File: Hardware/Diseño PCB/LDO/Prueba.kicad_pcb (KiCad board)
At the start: 2 copper layers, 100 x 100 mm, 55 parts, among them Q1 2N3904, Q10 BC557, Q11 BC547, Q12 BC557, Q13 2N3906, Q14 2N3904, Q15 2N3906, Q16 2N3904, Q17 2N3906, Q18 2N3904, Q19 2N3904, Q2 2N3904, Q3 2N3904, Q4 2N3906, Q5 2N3906, Q6 2N3904, Q7 2N3904, Q8 IRF4905, Q9 BC547, U1 TL431LP, U4 LM324

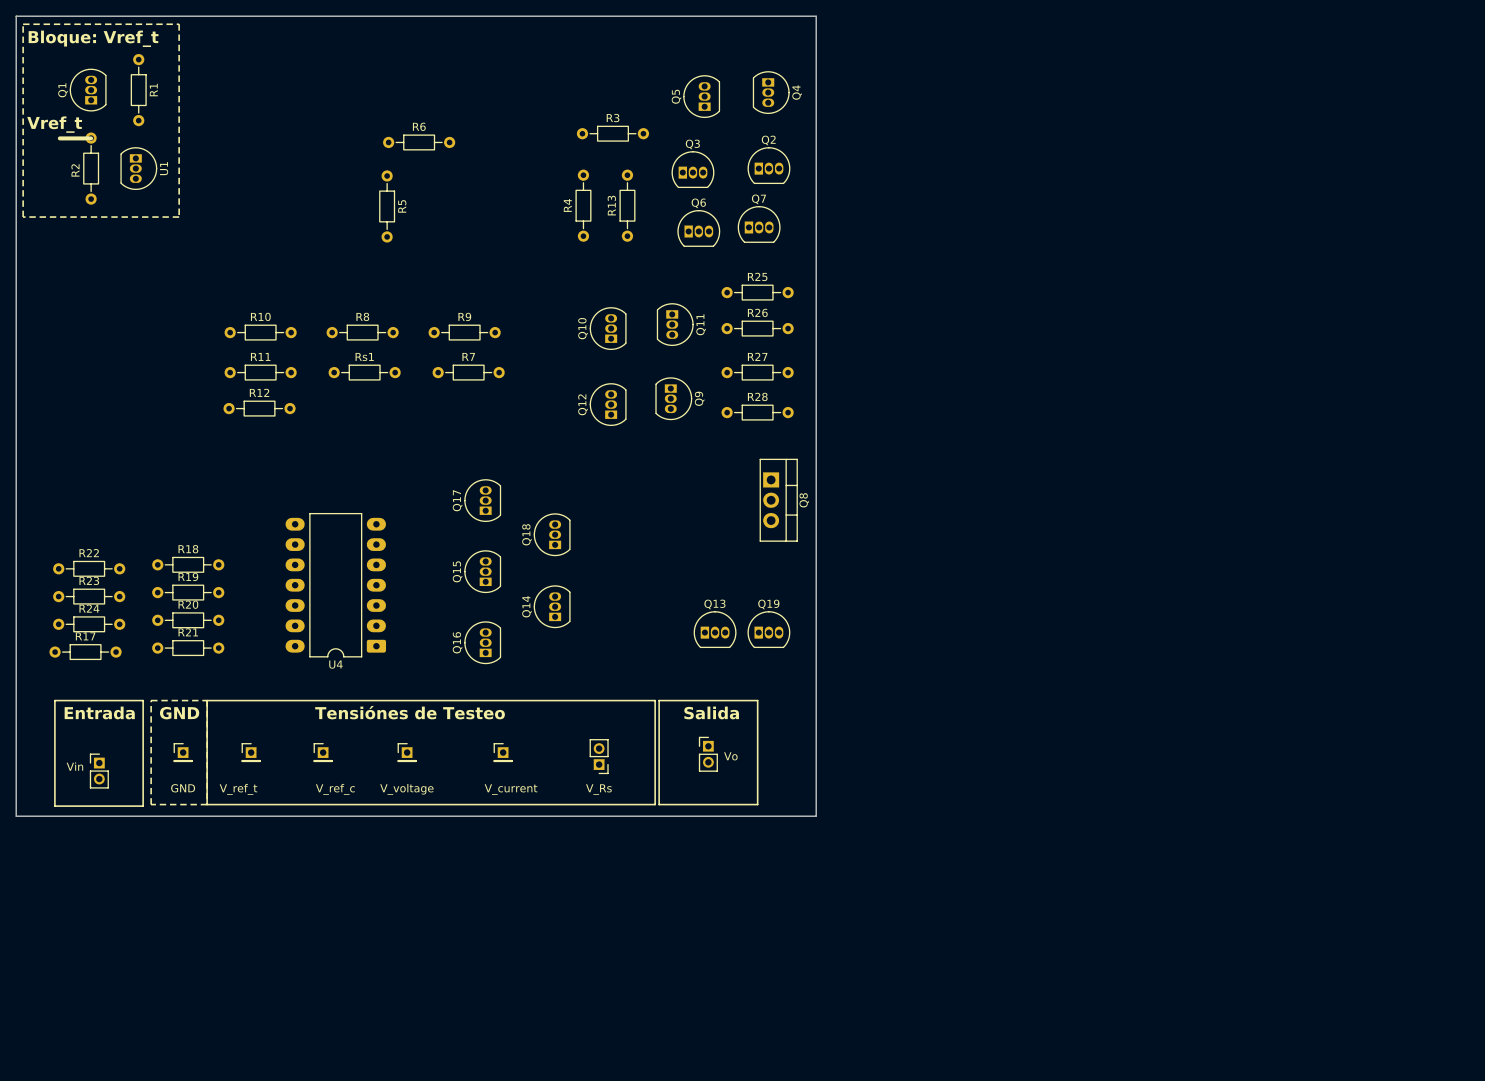
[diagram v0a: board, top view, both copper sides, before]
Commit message: Diseño PCB : Bloque testeos y Vref_t
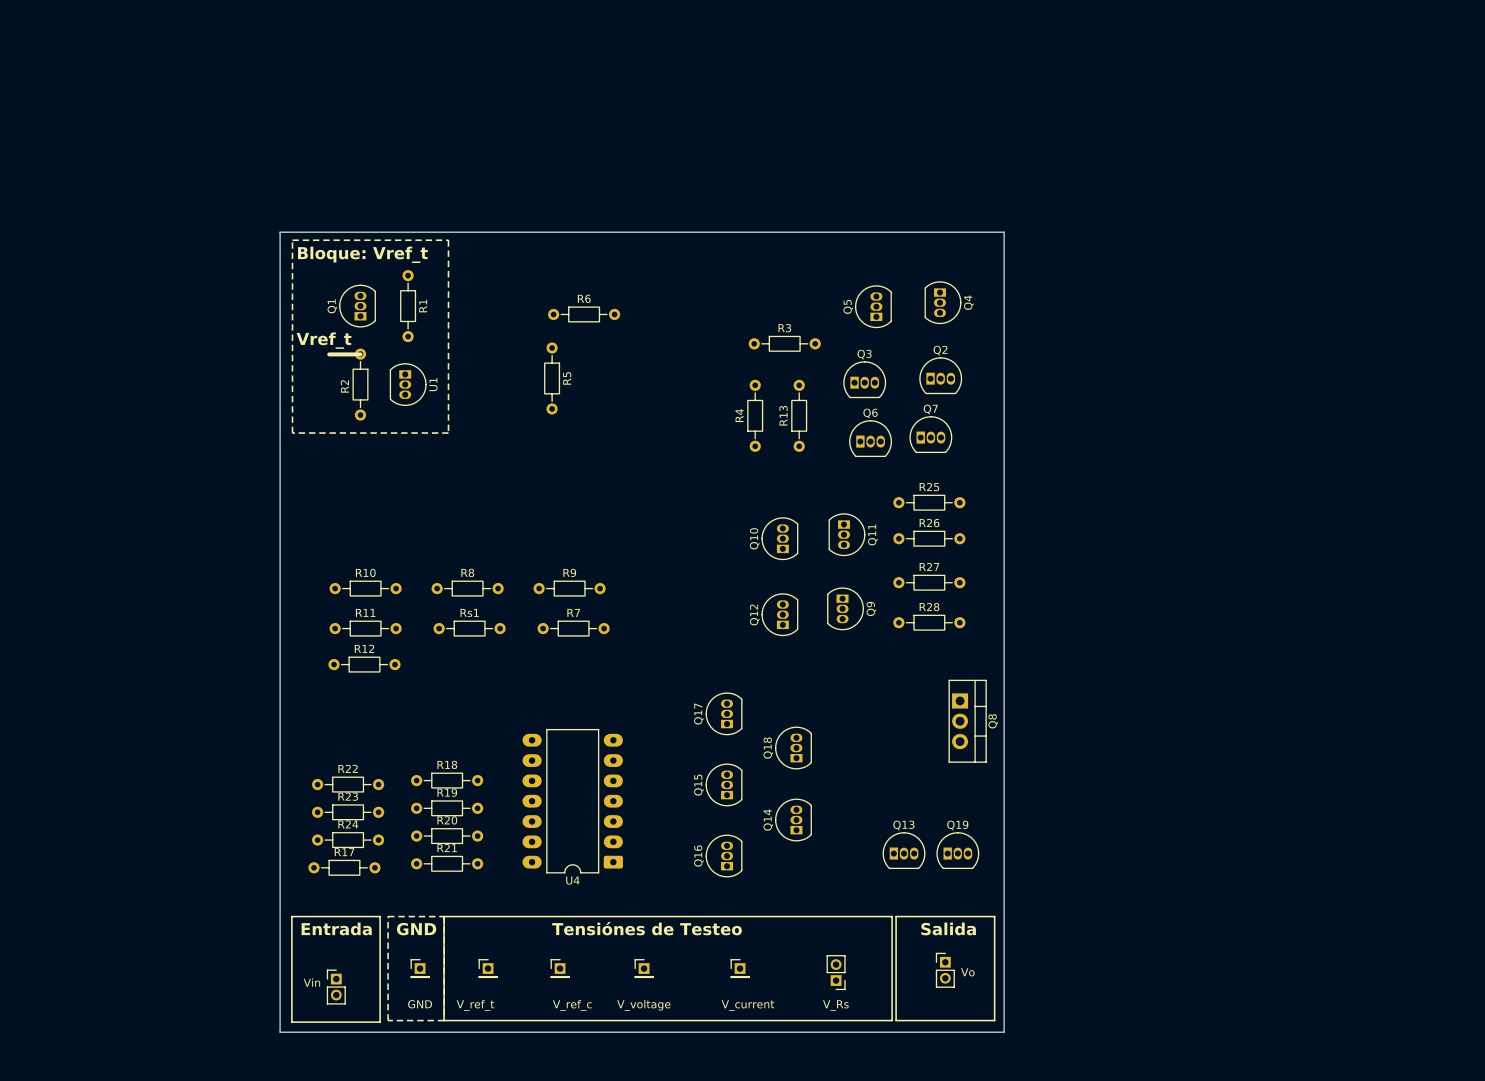
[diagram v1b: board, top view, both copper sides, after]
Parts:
- moved R1 43.2 mm to (118.6, 47.9)
- moved U1 43.2 mm to (118.3, 60.2)
- moved Q1 43.2 mm to (112.7, 53.0)
- moved R2 43.2 mm to (112.7, 57.7)
- moved R24 42.1 mm to (107.3, 118.4)
- moved R17 42.1 mm to (106.9, 121.9)
- moved R22 42.1 mm to (107.3, 111.5)
- moved R23 42.1 mm to (107.3, 115.0)
- moved R20 42.1 mm to (119.7, 117.9)
- moved R18 42.1 mm to (119.7, 111.0)
- moved R19 42.1 mm to (119.7, 114.5)
- moved R21 42.1 mm to (119.7, 121.4)
- moved Q15 40.3 mm to (158.5, 112.8)
- moved Q17 40.3 mm to (158.5, 103.9)
- moved Q14 40.3 mm to (167.2, 117.2)
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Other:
- board size 100 x 100 mm -> 90.5 x 100 mm

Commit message: Diseño PCB
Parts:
- moved R28 35.3 mm to (187.5, 56.8), turned to 90 degrees
- moved Q12 34.1 mm to (186.8, 65.0)
- moved R27 29.6 mm to (182.5, 56.8), turned to 90 degrees
- moved Q4 26.5 mm to (159.0, 45.5)
- moved R26 24.1 mm to (177.0, 56.8), turned to 90 degrees
- moved Q10 22.7 mm to (177.4, 62.7), turned to -90 degrees
- moved Q9 19.9 mm to (177.6, 69.0)
- moved Q6 18.3 mm to (158.8, 60.5)
- moved Q3 18.1 mm to (159.1, 51.6), turned to -90 degrees
- moved Q7 18.1 mm to (166.4, 60.5)
- moved R4 17.8 mm to (145.4, 62.9)
- moved R3 17.8 mm to (145.3, 50.1)
- moved Q2 17.1 mm to (168.1, 54.1), turned to 90 degrees
- moved R13 16.2 mm to (152.6, 62.9)
- moved Q11 15.6 mm to (186.8, 71.5), turned to 90 degrees
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
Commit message: Diseño PCB
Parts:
- moved R10 106.4 mm to (215.2, 75.0)
- moved R11 106.4 mm to (215.2, 80.0)
- moved R12 106.4 mm to (215.1, 84.5)
- moved R18 106.4 mm to (225.4, 99.0)
- moved R19 106.4 mm to (225.4, 102.5)
- moved R20 106.4 mm to (225.4, 105.9)
- moved R21 106.4 mm to (225.4, 109.4)
- moved R22 106.4 mm to (213.0, 99.5)
- moved R23 106.4 mm to (213.0, 103.0)
- moved R24 106.4 mm to (213.0, 106.4)
- moved R7 106.4 mm to (241.2, 80.0)
- moved R8 106.4 mm to (228.0, 75.0)
- moved R9 106.4 mm to (240.7, 75.0)
- moved Rs1 106.4 mm to (228.2, 80.0)
- moved U4 106.4 mm to (250.0, 109.2)
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
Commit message: Diseño PCB
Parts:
- moved R18 120.5 mm to (106.0, 115.0)
- moved LM324 119.4 mm to (130.6, 112.7)
- moved R12 115.0 mm to (106.0, 121.0)
- moved R9 113.6 mm to (136.8, 121.0)
- moved R7 107.4 mm to (140.0, 116.0)
- moved R23 107.3 mm to (106.0, 96.0)
- moved R11 107.2 mm to (116.2, 121.0)
- moved R24 107.1 mm to (106.0, 102.0)
- moved R17 106.6 mm to (106.0, 108.5)
- moved R20 104.8 mm to (121.8, 90.0)
- moved R10 100.2 mm to (126.2, 121.0)
- moved R8 94.2 mm to (140.0, 108.6)
- moved R19 85.9 mm to (140.4, 90.0), turned to 180 degrees
- moved R21 84.3 mm to (142.3, 95.0)
- moved Rs1 83.3 mm to (150.0, 108.5), turned to -90 degrees
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- renumbered U4 to LM324
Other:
- board size 90.5 x 100 mm -> 90.5 x 92.5 mm
- board text added: "Grupo 7: Regulador de baja caída (LDO,Low Dropout Regulator)"

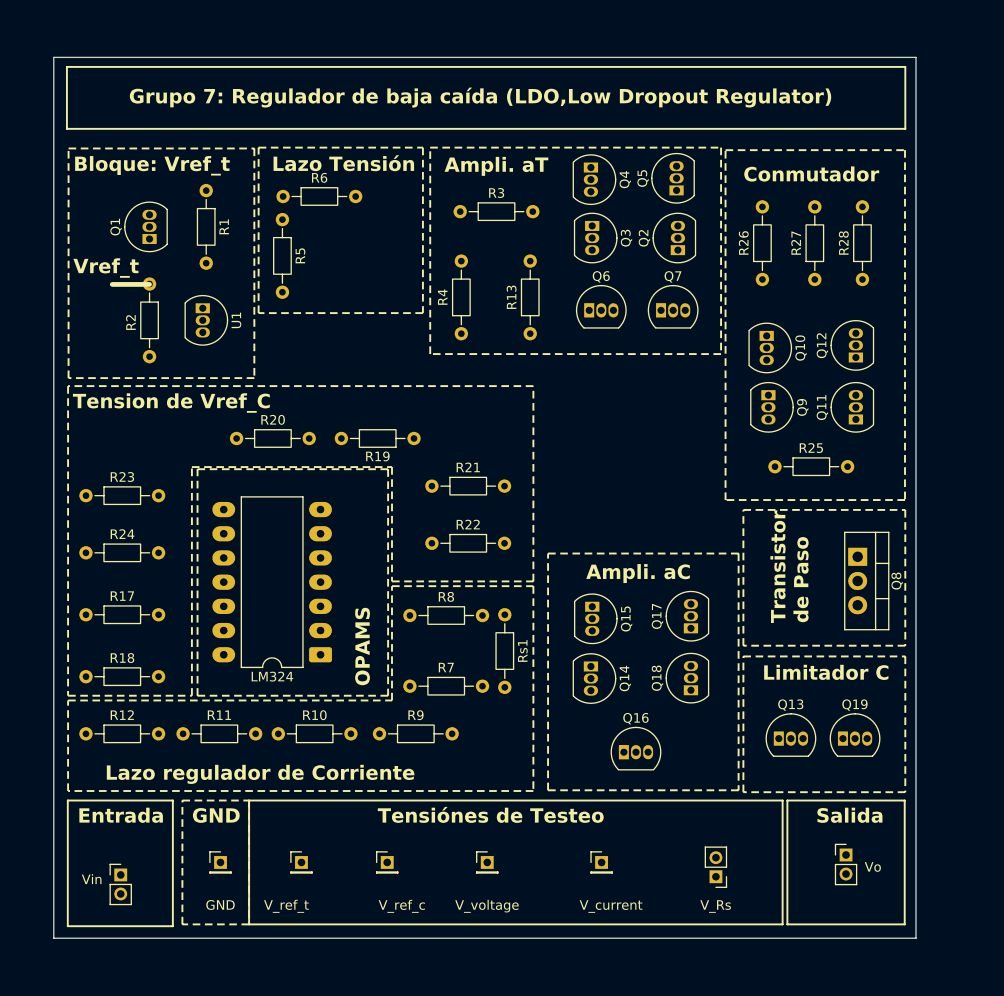
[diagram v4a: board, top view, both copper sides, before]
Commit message: Diseño PCB: Informe, orificos de sujeción
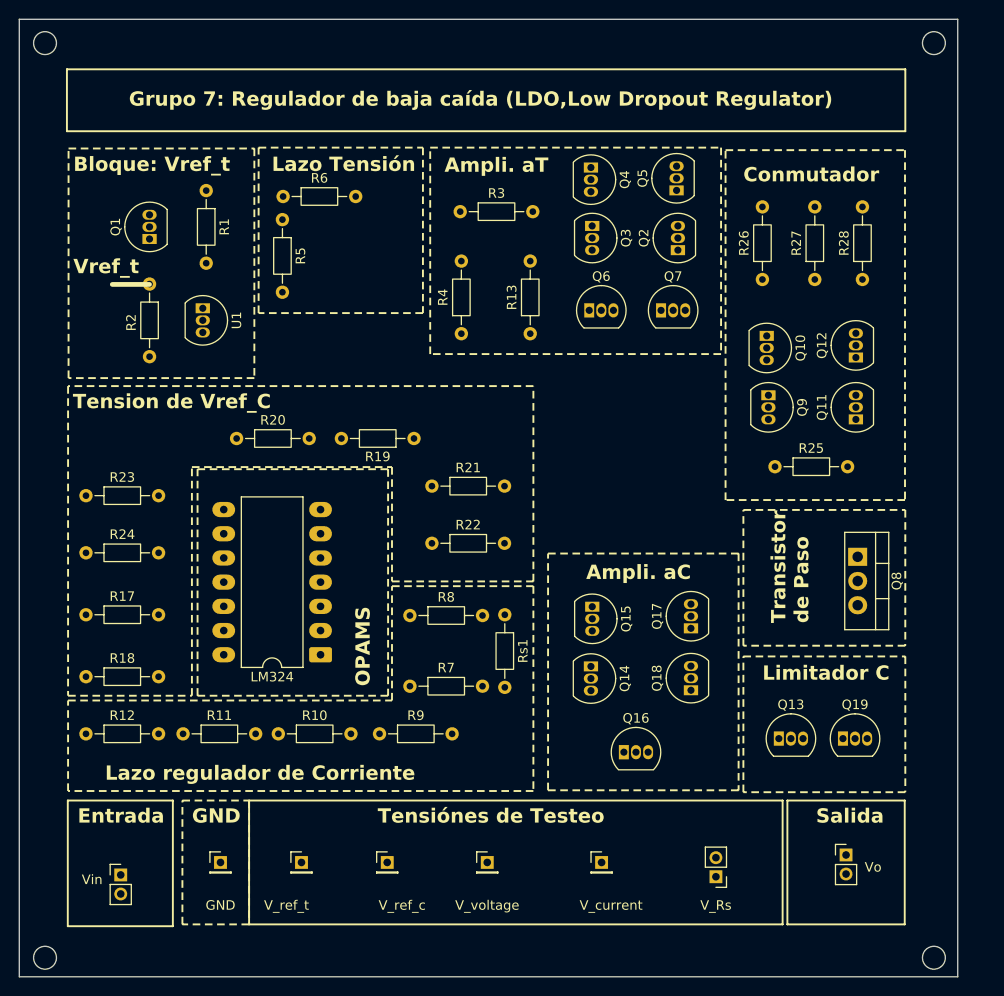
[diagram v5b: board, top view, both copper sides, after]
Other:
- board size 90.5 x 92.5 mm -> 98.5 x 100.5 mm
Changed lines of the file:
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@@
 	)
 	(gr_rect
-		(start 104 51)
-		(end 192 57.499999)
+		(start 104 51.25)
+		(end 192 57.749999)
 		(stroke
 			(width 0.2)
@@
 	)
 	(gr_rect
-		(start 102.619999 50)
-		(end 193.119999 142.45256)
+		(start 98.999999 46)
+		(end 197.499999 146.5)
 		(stroke
 			(width 0.05)
+			(type solid)
+		)
+		(fill no)
+		(layer "Edge.Cuts")
+	)
+	(gr_circle
+		(center 101.7 48.5)
+		(end 102.9 48.5)
+		(stroke
+			(width 0.1)
+			(type solid)
+		)
+		(fill no)
+		(layer "Edge.Cuts")
+	)
+	(gr_circle
+		(center 101.7 144.5)
+		(end 102.9 144.5)
+		(stroke
+			(width 0.1)
+			(type solid)
+		)
+		(fill no)
+		(layer "Edge.Cuts")
+	)
+	(gr_circle
+		(center 195 48.5)
+		(end 196.2 48.5)
+		(stroke
+			(width 0.1)
+			(type solid)
+		)
+		(fill no)
+		(layer "Edge.Cuts")
+	)
+	(gr_circle
+		(center 195 144.5)
+		(end 196.2 144.5)
+		(stroke
+			(width 0.1)
 			(type solid)
 		)
@@
 	)
 	(gr_text "Grupo 7: Regulador de baja caída (LDO,Low Dropout Regulator)"
-		(at 110.5 55 0)
-		(layer "F.SilkS")
-		(effects
+		(at 110.5 55.25 0)
+		(layer "F.SilkS")
+		(effects

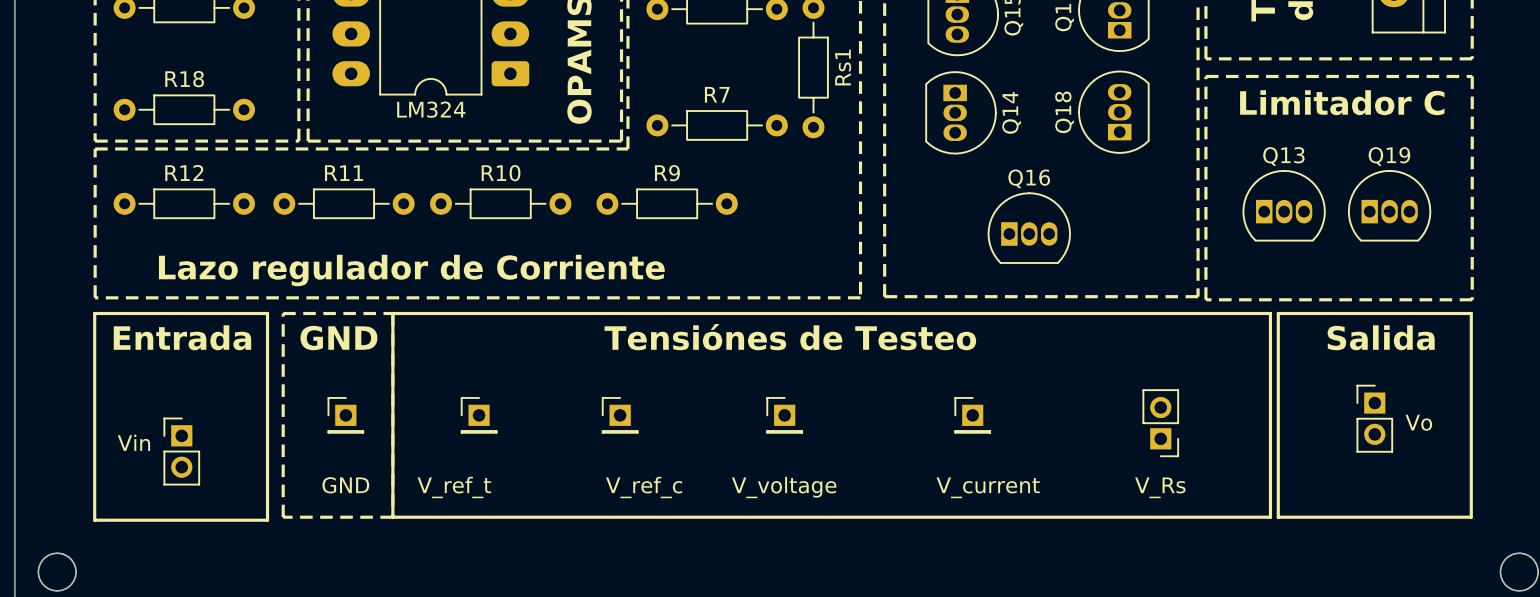
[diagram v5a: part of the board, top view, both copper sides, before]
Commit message: Diseño PCB: Transistores BC557/BC547 en esquematico y pcb
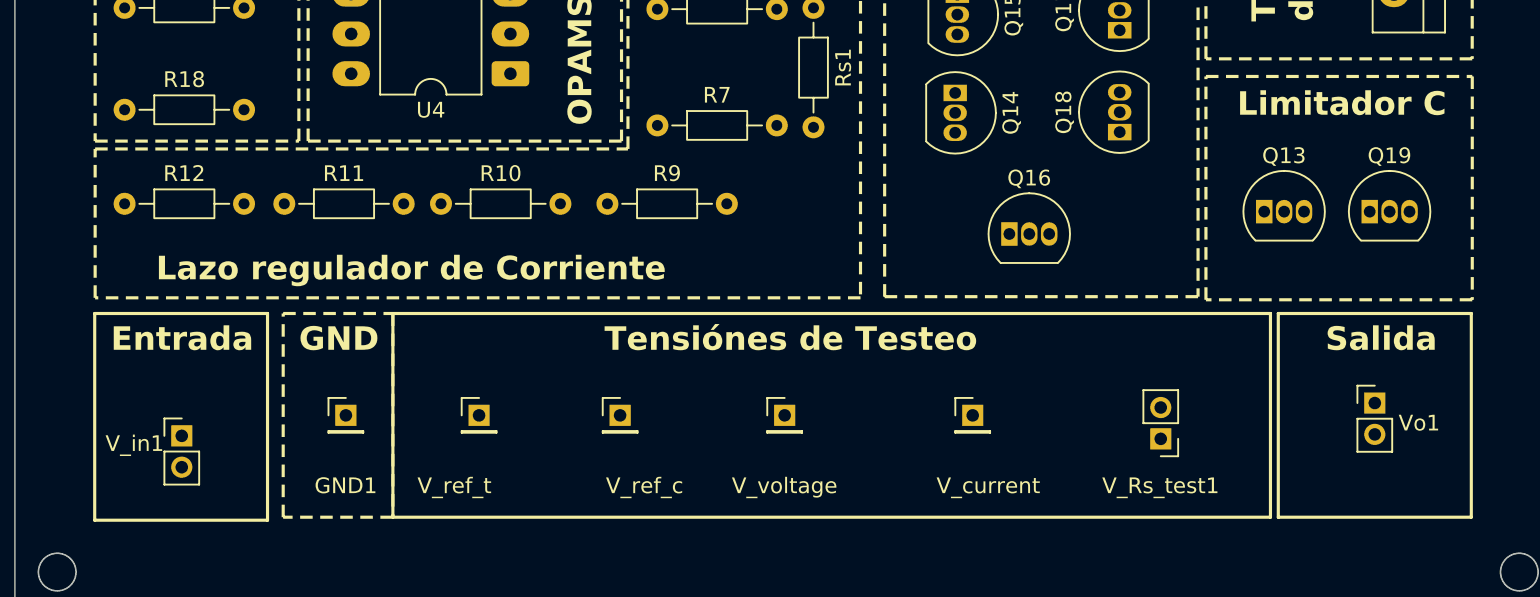
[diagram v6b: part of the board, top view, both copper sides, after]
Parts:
- Q13, Q15, Q17, Q4, Q5: value 2N3906 -> BC557
- Q14, Q16, Q18, Q19, Q2, Q3, Q6, Q7: value 2N3904 -> BC547
- renumbered GND to GND1, LM324 to U4, V_Rs to V_Rs_test1, Vin to V_in1, Vo to Vo1
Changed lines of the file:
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@@
 			)
 		)
-		(property "Value" "2N3906"
+		(property "Value" "BC557"
 			(at 1.27 2.79 0)
 			(layer "F.Fab")
@@
 		(descr "14-lead though-hole mounted DIP package, row spacing 10.16mm (400 mils), LongPads")
 		(tags "THT DIP DIL PDIP 2.54mm 10.16mm 400mil LongPads")
-		(property "Reference" "LM324"
+		(property "Reference" "U4"
 			(at 5.08 -2.33 0)
 			(layer "F.SilkS")
@@
 			)
 		)
-		(property "Value" "2N3904"
+		(property "Value" "BC547"
 			(at 1.27 2.79 0)
 			(layer "F.Fab")
@@
 		(descr "Through hole straight pin header, 1x02, 2.00mm pitch, single row")
 		(tags "Through hole pin header THT 1x02 2.00mm single row")
-		(property "Reference" "Vo"
+		(property "Reference" "Vo1"
 			(at 2.841551 1.28537 180)
 			(layer "F.SilkS")
@@
 			)
 		)
-		(property "Value" "2N3904"
+		(property "Value" "BC547"
 			(at 1.27 2.79 90)
 			(layer "F.Fab")
@@
 			)
 		)
-		(property "Value" "2N3904"
+		(property "Value" "BC547"
 			(at 1.27 2.79 90)
 			(layer "F.Fab")
@@
 			)
 		)
-		(property "Value" "2N3906"
+		(property "Value" "BC557"
 			(at 1.27 2.79 90)
 			(layer "F.Fab")
@@
 		(descr "Through hole straight pin header, 1x02, 2.00mm pitch, single row")
 		(tags "Through hole pin header THT 1x02 2.00mm single row")
-		(property "Reference" "Vin"
+		(property "Reference" "V_in1"
 			(at -3 0.5 0)
 			(layer "F.SilkS")
@@
 			)
 		)
-		(property "Value" "2N3904"
+		(property "Value" "BC547"
 			(at 1.27 2.79 0)
 			(layer "F.Fab")
@@
 			)
 		)
-		(property "Value" "2N3904"
+		(property "Value" "BC547"
 			(at 1.27 2.79 90)
 			(layer "F.Fab")
@@
 			)
 		)
-		(property "Value" "2N3904"
+		(property "Value" "BC547"
 			(at 1.27 2.79 0)
 			(layer "F.Fab")
@@
 			)
 		)
-		(property "Value" "2N3906"
+		(property "Value" "BC557"
 			(at 1.27 2.79 90)
 			(layer "F.Fab")
@@
 			)
 		)
-		(property "Value" "2N3904"
+		(property "Value" "BC547"
 			(at 1.27 2.79 0)
 			(layer "F.Fab")
@@
 			)
 		)
-		(property "Value" "2N3904"
+		(property "Value" "BC547"
 			(at 1.27 2.79 90)
 			(layer "F.Fab")
@@
 		(descr "Through hole straight pin header, 1x01, 2.00mm pitch, single row")
 		(tags "Through hole pin header THT 1x01 2.00mm single row")
-		(property "Reference" "GND"
+		(property "Reference" "GND1"
 			(at 0 4.5 0)
 			(layer "F.SilkS")
@@
 		(descr "Through hole straight pin header, 1x02, 2.00mm pitch, single row")
 		(tags "Through hole pin header THT 1x02 2.00mm single row")
-		(property "Reference" "V_Rs"
+		(property "Reference" "V_Rs_test1"
 			(at 0 -3 0)
 			(layer "F.SilkS")
@@
 			)
 		)
-		(property "Value" "2N3906"
+		(property "Value" "BC557"
 			(at 1.27 2.79 90)
 			(layer "F.Fab")
@@
 			)
 		)
-		(property "Value" "2N3906"
+		(property "Value" "BC557"
 			(at 1.27 2.79 90)
 			(layer "F.Fab")
